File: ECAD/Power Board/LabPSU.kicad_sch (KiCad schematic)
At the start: 74 parts, among them J1 DC-IN, J2 CTRL, J3 UPDI, J4 +, J5 -, Q1 Si7454FDP, Q2 Si7454FDP, U1 LM2594HVN-5.0, U2 LM5118MH, U3 LM358, U4 ATtiny414-SS, U5 MCP4811, U6 INA286

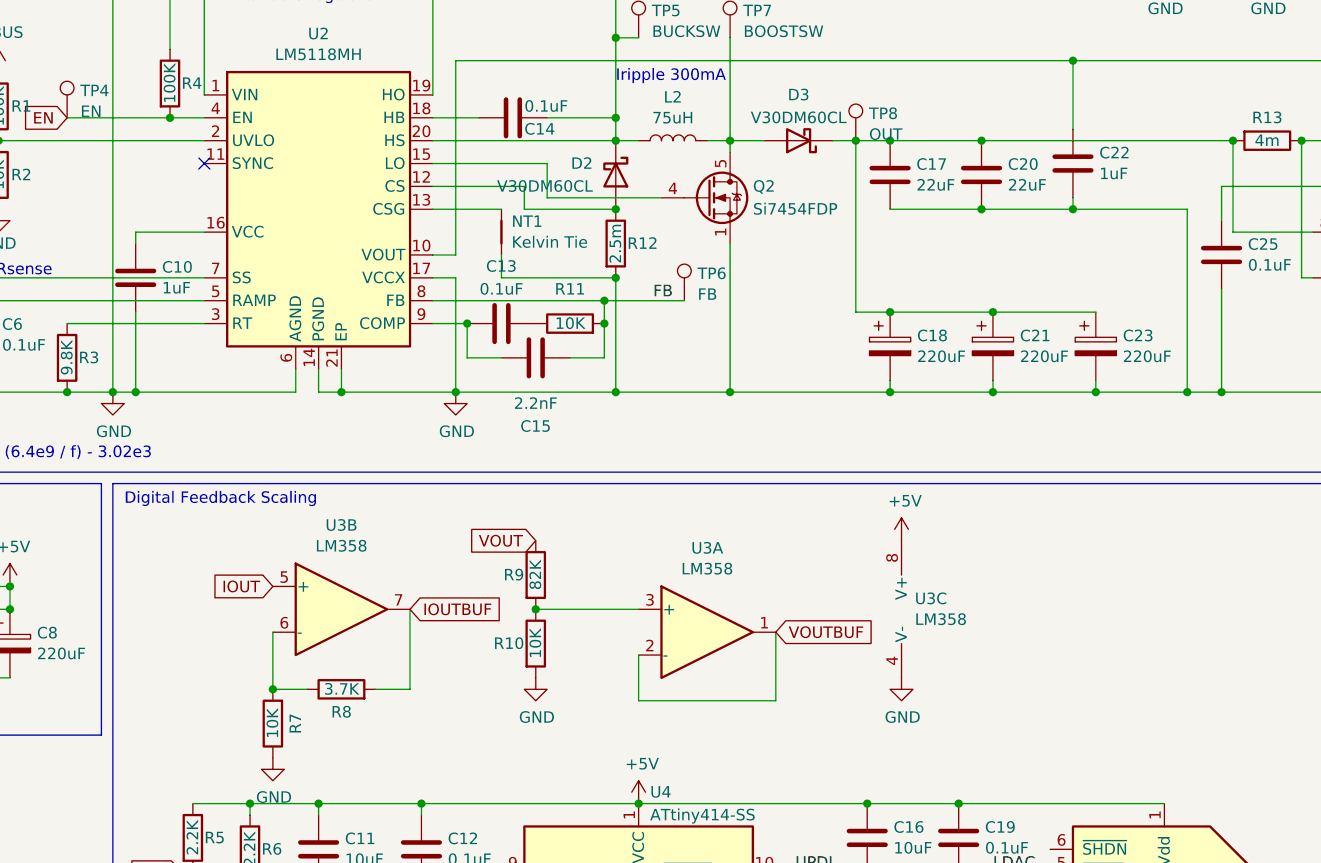
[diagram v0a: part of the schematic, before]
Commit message: Update component values with actually used values
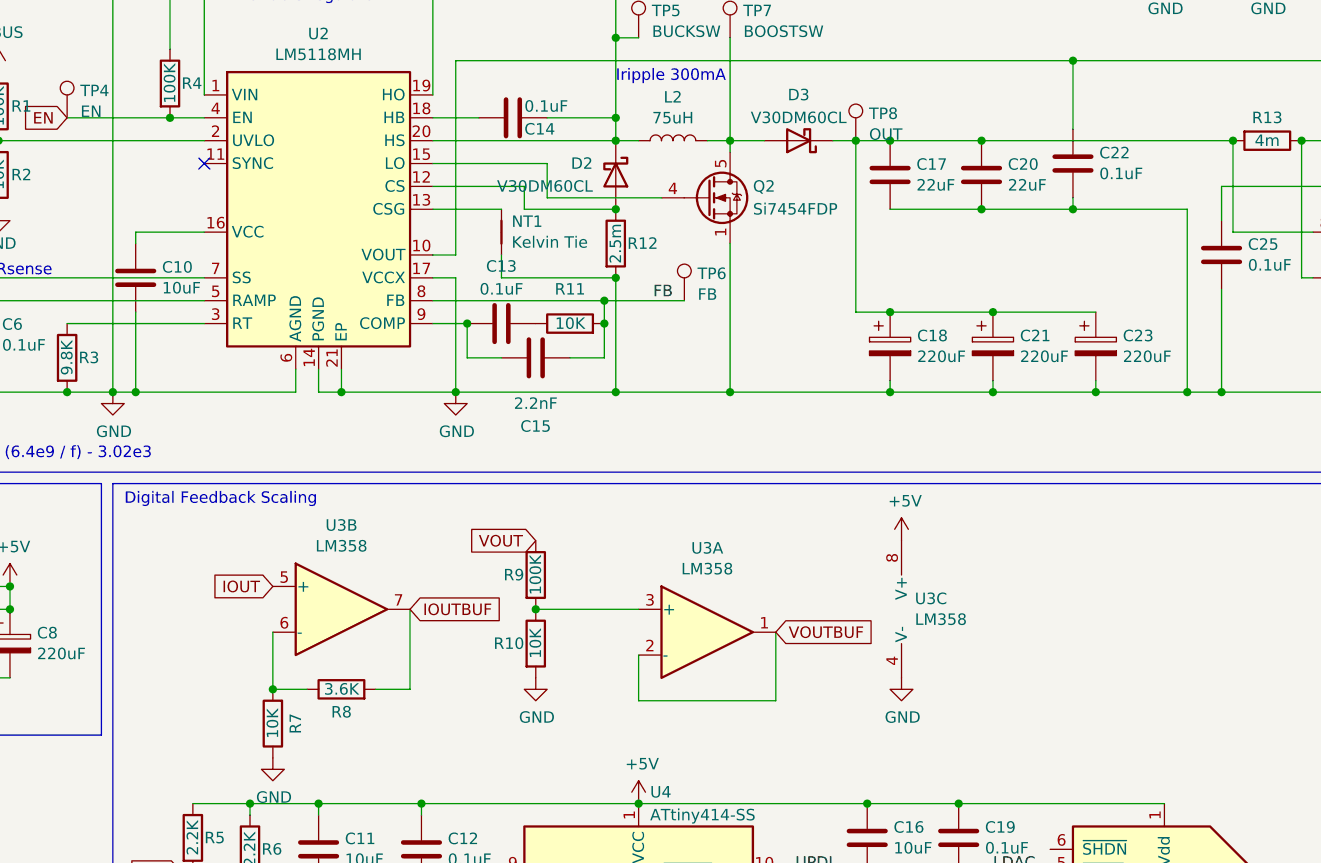
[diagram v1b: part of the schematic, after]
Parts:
- C10: value 1uF -> 10uF
- C22: value 1uF -> 0.1uF
- R8: value 3.7K -> 3.6K
- R9: value 82K -> 100K
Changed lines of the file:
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@@
       (effects (font (size 1.27 1.27)) (justify left))
     )
-    (property "Value" "1uF" (id 1) (at 85.471 70.993 0)
+    (property "Value" "10uF" (id 1) (at 85.471 70.993 0)
       (effects (font (size 1.27 1.27)) (justify left))
     )
@@
       (effects (font (size 1.27 1.27)) (justify left))
     )
-    (property "Value" "1uF" (id 1) (at 189.611 58.293 0)
+    (property "Value" "0.1uF" (id 1) (at 189.611 58.293 0)
       (effects (font (size 1.27 1.27)) (justify left))
     )
@@
       (effects (font (size 1.27 1.27)) (justify right))
     )
-    (property "Value" "82K" (id 1) (at 127 102.87 90))
+    (property "Value" "100K" (id 1) (at 127 102.87 90))
     (property "Footprint" "Resistor_SMD:R_0805_2012Metric" (id 2) (at 125.222 102.87 90)
       (effects (font (size 1.27 1.27)) hide)
@@
     (in_bom yes) (on_board yes)
     (property "Reference" "R8" (id 0) (at 105.41 118.11 90))
-    (property "Value" "3.7K" (id 1) (at 105.41 115.57 90))
+    (property "Value" "3.6K" (id 1) (at 105.41 115.57 90))
     (property "Footprint" "Resistor_SMD:R_0805_2012Metric" (id 2) (at 105.41 117.348 90)
       (effects (font (size 1.27 1.27)) hide)
@@
     )
     (path "/00000000-0000-0000-0000-000061bffccd"
-      (reference "C10") (unit 1) (value "1uF") (footprint "Capacitor_SMD:C_0805_2012Metric")
+      (reference "C10") (unit 1) (value "10uF") (footprint "Capacitor_SMD:C_0805_2012Metric")
     )
     (path "/00000000-0000-0000-0000-0000621edfa9"
@@
     )
     (path "/00000000-0000-0000-0000-000061c3707f"
-      (reference "C22") (unit 1) (value "1uF") (footprint "Capacitor_SMD:C_0805_2012Metric")
+      (reference "C22") (unit 1) (value "0.1uF") (footprint "Capacitor_SMD:C_0805_2012Metric")
     )
     (path "/00000000-0000-0000-0000-000061f123d7"
@@
     )
     (path "/00000000-0000-0000-0000-0000622b028c"
-      (reference "R8") (unit 1) (value "3.7K") (footprint "Resistor_SMD:R_0805_2012Metric")
+      (reference "R8") (unit 1) (value "3.6K") (footprint "Resistor_SMD:R_0805_2012Metric")
     )
     (path "/00000000-0000-0000-0000-000061c561c4"
-      (reference "R9") (unit 1) (value "82K") (footprint "Resistor_SMD:R_0805_2012Metric")
+      (reference "R9") (unit 1) (value "100K") (footprint "Resistor_SMD:R_0805_2012Metric")
     )
     (path "/00000000-0000-0000-0000-000061f1d569"
